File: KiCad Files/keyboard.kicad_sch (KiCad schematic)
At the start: 193 parts, among them J2 Button, J3 78171-0004, J5 Conn_01x03_Male, U1 SOT-23-5 5.5V 3.3V 500mA, U2 RP2040, Y1 3225_4P 12MHz

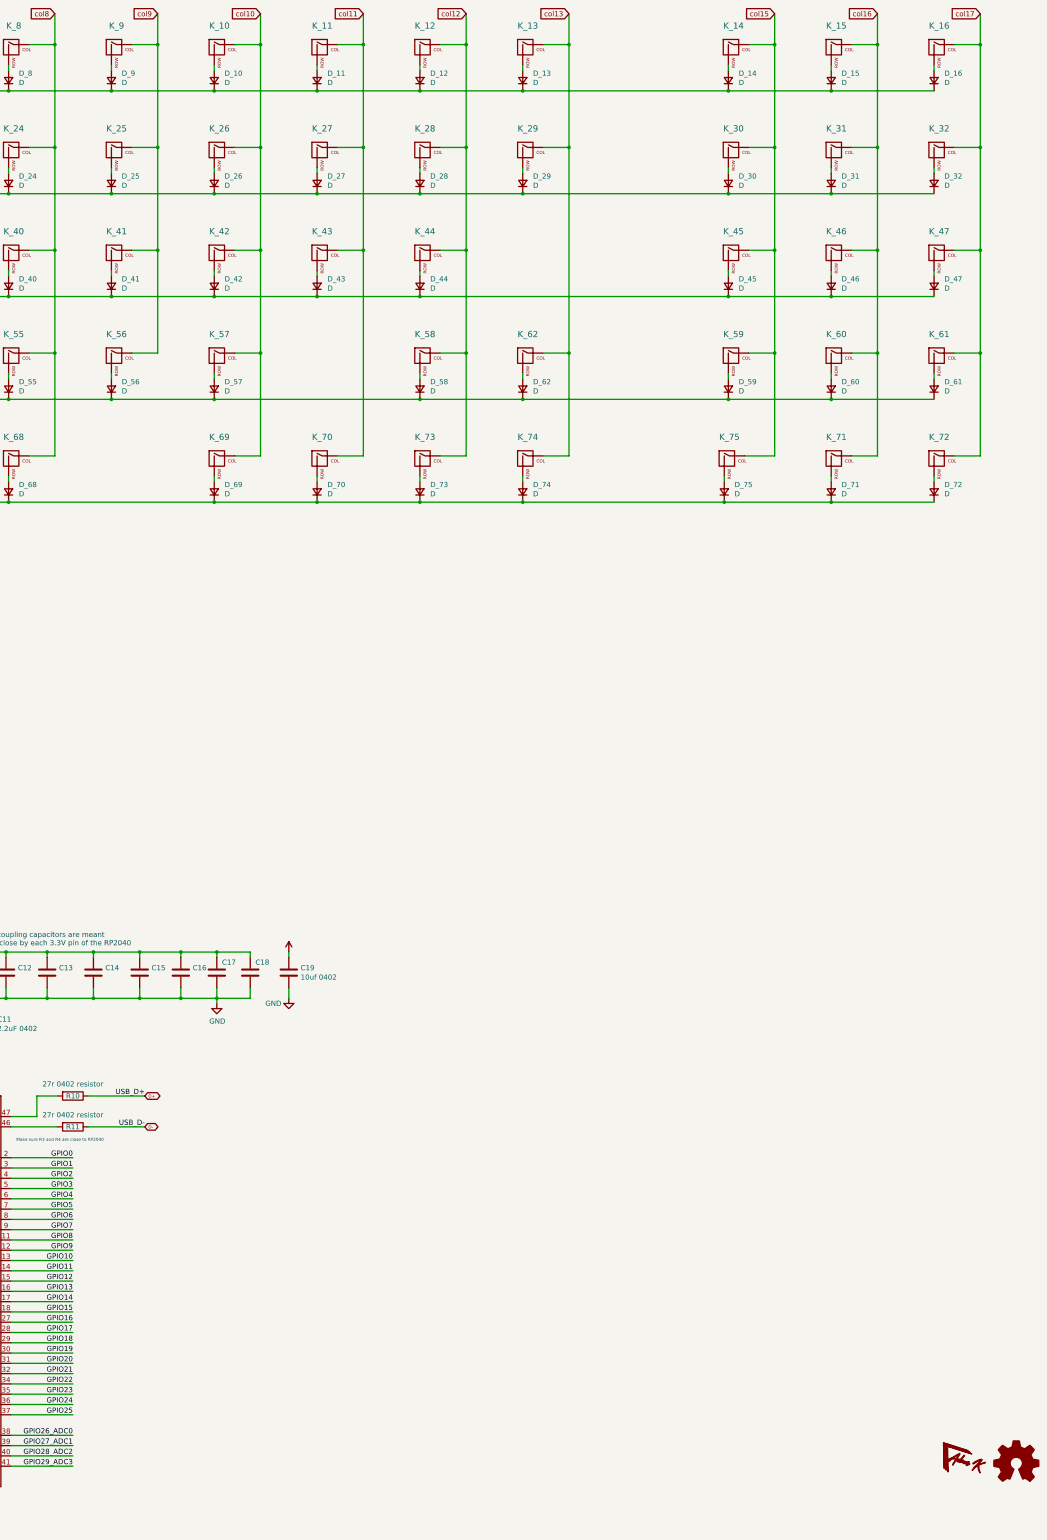
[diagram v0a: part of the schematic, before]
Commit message: routed matrix and updated git ignore
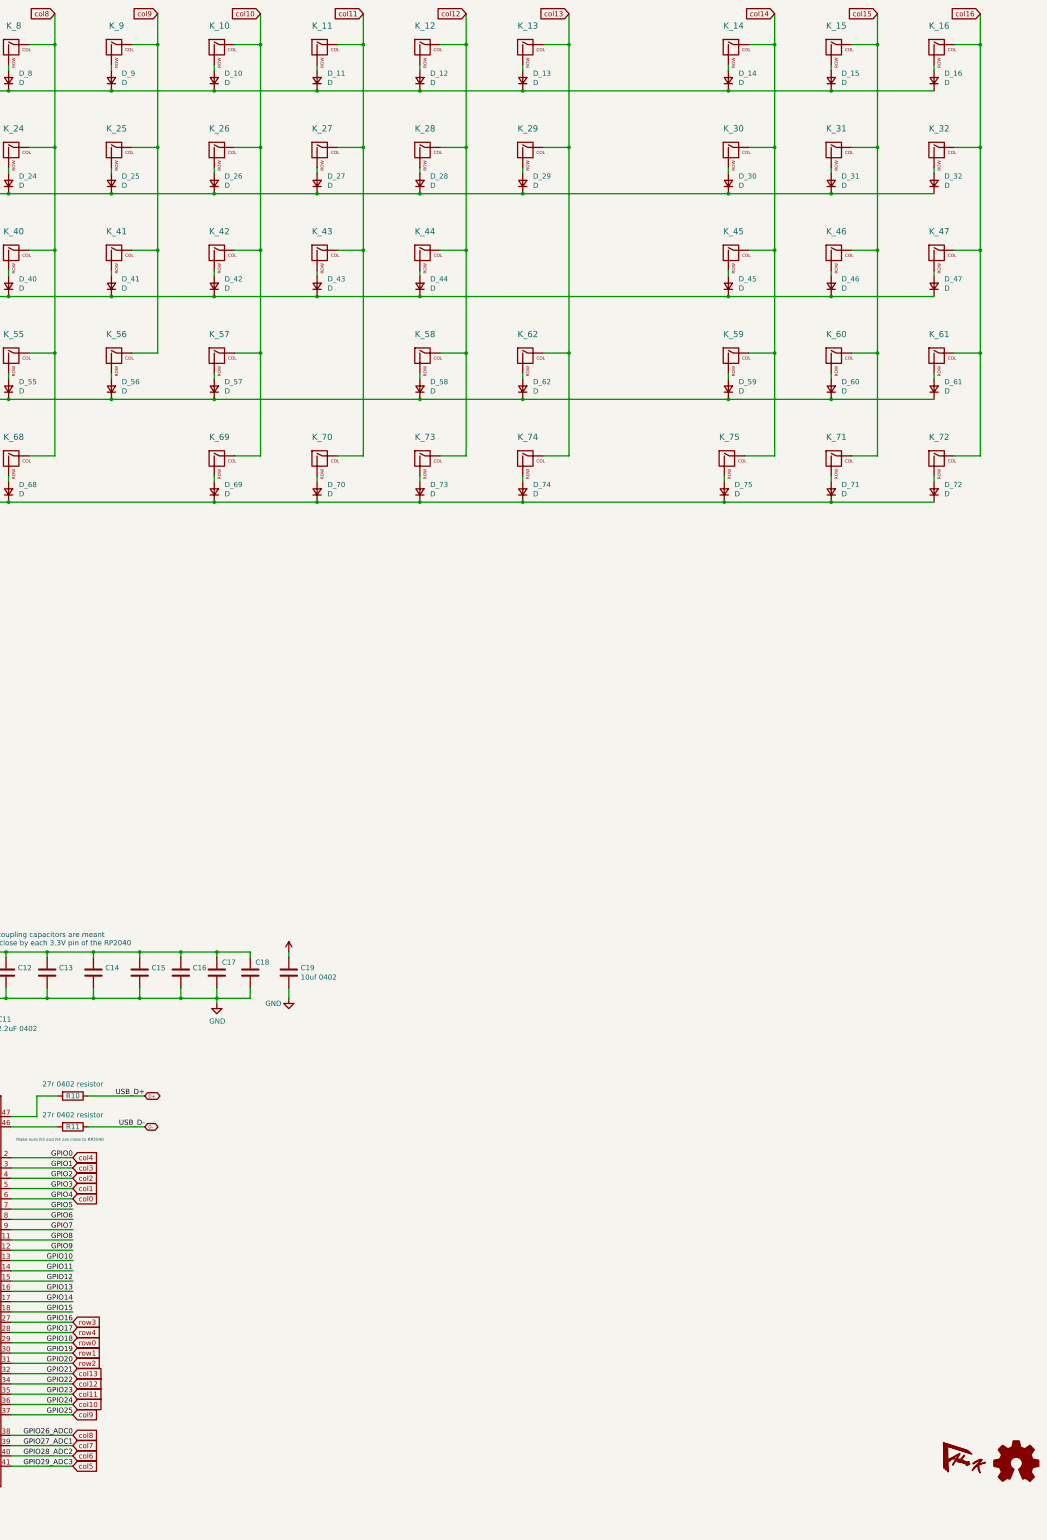
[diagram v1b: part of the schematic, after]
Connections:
- net GPIO0 is gone; now on net col4: U2.2 (GPIO0)
- net GPIO1 is gone; now on net col3: U2.3 (GPIO1)
- net GPIO16 is gone; now on net row3: U2.27 (GPIO16)
- net GPIO17 is gone; now on net row4: U2.28 (GPIO17)
- net GPIO18 is gone; now on net row0: U2.29 (GPIO18)
- net GPIO19 is gone; now on net row1: U2.30 (GPIO19)
- net GPIO2 is gone; now on net col2: U2.4 (GPIO2)
- net GPIO20 is gone; now on net row2: U2.31 (GPIO20)
- net GPIO21 is gone; now on net col13: U2.32 (GPIO21)
- net GPIO22 is gone; now on net col12: U2.34 (GPIO22)
- net GPIO23 is gone; now on net col11: U2.35 (GPIO23)
- net GPIO24 is gone; now on net col10: U2.36 (GPIO24)
- net GPIO25 is gone; now on net col9: U2.37 (GPIO25)
- net GPIO26_ADC0 is gone; now on net col8: U2.38 (GPIO26_ADC0)
- net GPIO27_ADC1 is gone; now on net col7: U2.39 (GPIO27_ADC1)
- net GPIO28_ADC2 is gone; now on net col6: U2.40 (GPIO28_ADC2)
- net GPIO29_ADC3 is gone; now on net col5: U2.41 (GPIO29_ADC3)
- net GPIO3 is gone; now on net col1: U2.5 (GPIO3)
- net GPIO4 is gone; now on net col0: U2.6 (GPIO4)
- net col17 is gone; now on net col16: K_16.1 (COL), K_32.1 (COL), K_47.1 (COL), K_61.1 (COL), K_72.1 (COL)
- net col15: now also K_15.1 (COL), K_31.1 (COL), K_46.1 (COL), K_60.1 (COL), K_71.1 (COL); no longer K_14.1 (COL), K_30.1 (COL), K_45.1 (COL), K_59.1 (COL), K_75.1 (COL)
- net col16: no longer K_15.1 (COL), K_31.1 (COL), K_46.1 (COL), K_60.1 (COL), K_71.1 (COL)
- new net col14: K_14.1 (COL), K_30.1 (COL), K_45.1 (COL), K_59.1 (COL), K_75.1 (COL)
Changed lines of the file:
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@@
     (effects (font (size 1.27 1.27)) (justify right bottom))
   )
+  (global_label "col12" (shape input) (at 262.255 365.125 0)
+    (effects (font (size 1.27 1.27)) (justify left))
+    (property "Intersheetrefs" "${INTERSHEET_REFS}" (at 262.255 365.125 0)
+      (effects (font (size 1.27 1.27)) hide)
+    )
+  )
   (global_label "col11" (shape input) (at 334.01 26.67 180)
     (effects (font (size 1.27 1.27)) (justify right))
@@
     )
   )
+  (global_label "row2" (shape input) (at 262.255 360.045 0)
+    (effects (font (size 1.27 1.27)) (justify left))
+    (property "Intersheetrefs" "${INTERSHEET_REFS}" (at 262.255 360.045 0)
+      (effects (font (size 1.27 1.27)) hide)
+    )
+  )
   (global_label "col1" (shape input) (at 80.01 26.67 180)
     (effects (font (size 1.27 1.27)) (justify right))
@@
     (effects (font (size 1.27 1.27)) (justify right))
     (property "Intersheetrefs" "${INTERSHEET_REFS}" (at 130.81 26.67 0)
+      (effects (font (size 1.27 1.27)) hide)
+    )
+  )
+  (global_label "col0" (shape input) (at 262.255 319.405 0)
+    (effects (font (size 1.27 1.27)) (justify left))
+    (property "Intersheetrefs" "${INTERSHEET_REFS}" (at 262.255 319.405 0)
       (effects (font (size 1.27 1.27)) hide)
     )
@@
     )
   )
+  (global_label "row4" (shape input) (at 262.255 352.425 0)
+    (effects (font (size 1.27 1.27)) (justify left))
+    (property "Intersheetrefs" "${INTERSHEET_REFS}" (at 262.255 352.425 0)
+      (effects (font (size 1.27 1.27)) hide)
+    )
+  )
   (global_label "D-" (shape bidirectional) (at 280.035 301.625 0) (fields_autoplaced)
     (effects (font (size 0.762 0.762)) (justify left))
@@
     )
   )
+  (global_label "col6" (shape input) (at 262.255 382.905 0)
+    (effects (font (size 1.27 1.27)) (justify left))
+    (property "Intersheetrefs" "${INTERSHEET_REFS}" (at 262.255 382.905 0)
+      (effects (font (size 1.27 1.27)) hide)
+    )
+  )
   (global_label "col13" (shape input) (at 384.81 26.67 180)
     (effects (font (size 1.27 1.27)) (justify right))
@@
     )
   )
-  (global_label "col17" (shape input) (at 486.41 26.67 180)
+  (global_label "col1" (shape input) (at 262.255 316.865 0)
+    (effects (font (size 1.27 1.27)) (justify left))
+    (property "Intersheetrefs" "${INTERSHEET_REFS}" (at 262.255 316.865 0)
+      (effects (font (size 1.27 1.27)) hide)
+    )
+  )
+  (global_label "col16" (shape input) (at 486.41 26.67 180)
     (effects (font (size 1.27 1.27)) (justify right))
     (property "Intersheetrefs" "${INTERSHEET_REFS}" (at 486.41 26.67 0)
@@
     (property "Intersheetrefs" "${INTERSHEET_REFS}" (at 283.7108 294.005 0)
       (effects (font (size 0.762 0.762)) (justify left) hide)
+    )
+  )
+  (global_label "col7" (shape input) (at 262.255 380.365 0)
+    (effects (font (size 1.27 1.27)) (justify left))
+    (property "Intersheetrefs" "${INTERSHEET_REFS}" (at 262.255 380.365 0)
+      (effects (font (size 1.27 1.27)) hide)
     )
   )
@@
     )
   )
+  (global_label "col8" (shape input) (at 262.255 377.825 0)
+    (effects (font (size 1.27 1.27)) (justify left))
+    (property "Intersheetrefs" "${INTERSHEET_REFS}" (at 262.255 377.825 0)
+      (effects (font (size 1.27 1.27)) hide)
+    )
+  )
   (global_label "XIN" (shape input) (at 85.725 383.54 0) (fields_autoplaced)
     (effects (font (size 1.27 1.27)) (justify left))
@@
     )
   )
+  (global_label "col2" (shape input) (at 262.255 314.325 0)
+    (effects (font (size 1.27 1.27)) (justify left))
+    (property "Intersheetrefs" "${INTERSHEET_REFS}" (at 262.255 314.325 0)
+      (effects (font (size 1.27 1.27)) hide)
+    )
+  )
   (global_label "row3" (shape input) (at 31.75 121.92 180)
     (effects (font (size 1.27 1.27)) (justify right))
@@
     )
   )
-  (global_label "col15" (shape input) (at 435.61 26.67 180)
+  (global_label "col14" (shape input) (at 435.61 26.67 180)
     (effects (font (size 1.27 1.27)) (justify right))
     (property "Intersheetrefs" "${INTERSHEET_REFS}" (at 435.61 26.67 0)
@@
     )
   )
-  (global_label "col16" (shape input) (at 461.01 26.67 180)
+  (global_label "row3" (shape input) (at 262.255 349.885 0)
+    (effects (font (size 1.27 1.27)) (justify left))
+    (property "Intersheetrefs" "${INTERSHEET_REFS}" (at 262.255 349.885 0)
+      (effects (font (size 1.27 1.27)) hide)
+    )
+  )
+  (global_label "col3" (shape input) (at 262.255 311.785 0)
+    (effects (font (size 1.27 1.27)) (justify left))
+    (property "Intersheetrefs" "${INTERSHEET_REFS}" (at 262.255 311.785 0)
+      (effects (font (size 1.27 1.27)) hide)
+    )
+  )
+  (global_label "col11" (shape input) (at 262.255 367.665 0)
+    (effects (font (size 1.27 1.27)) (justify left))
+    (property "Intersheetrefs" "${INTERSHEET_REFS}" (at 262.255 367.665 0)
+      (effects (font (size 1.27 1.27)) hide)
+    )
+  )
+  (global_label "col10" (shape input) (at 262.255 370.205 0)
+    (effects (font (size 1.27 1.27)) (justify left))
+    (property "Intersheetrefs" "${INTERSHEET_REFS}" (at 262.255 370.205 0)
+      (effects (font (size 1.27 1.27)) hide)
+    )
+  )
+  (global_label "col15" (shape input) (at 461.01 26.67 180)
     (effects (font (size 1.27 1.27)) (justify right))
     (property "Intersheetrefs" "${INTERSHEET_REFS}" (at 461.01 26.67 0)
@@
     )
   )
+  (global_label "row1" (shape input) (at 262.255 357.505 0)
+    (effects (font (size 1.27 1.27)) (justify left))
+    (property "Intersheetrefs" "${INTERSHEET_REFS}" (at 262.255 357.505 0)
+      (effects (font (size 1.27 1.27)) hide)
+    )
+  )
+  (global_label "col9" (shape input) (at 262.255 372.745 0)
+    (effects (font (size 1.27 1.27)) (justify left))
+    (property "Intersheetrefs" "${INTERSHEET_REFS}" (at 262.255 372.745 0)
+      (effects (font (size 1.27 1.27)) hide)
+    )
+  )
   (global_label "row2" (shape input) (at 31.75 96.52 180)
     (effects (font (size 1.27 1.27)) (justify right))
@@
     )
   )
+  (global_label "col5" (shape input) (at 262.255 385.445 0)
+    (effects (font (size 1.27 1.27)) (justify left))
+    (property "Intersheetrefs" "${INTERSHEET_REFS}" (at 262.255 385.445 0)
+      (effects (font (size 1.27 1.27)) hide)
+    )
+  )
   (global_label "5V" (shape input) (at 35.56 228.6 90) (fields_autoplaced)
     (effects (font (size 0.762 0.762)) (justify left))
     (property "Intersheetrefs" "${INTERSHEET_REFS}" (at 35.56 225.8223 90)
       (effects (font (size 0.762 0.762)) (justify left) hide)
+    )
+  )
+  (global_label "col13" (shape input) (at 262.255 362.585 0)
+    (effects (font (size 1.27 1.27)) (justify left))
+    (property "Intersheetrefs" "${INTERSHEET_REFS}" (at 262.255 362.585 0)
+      (effects (font (size 1.27 1.27)) hide)
     )
   )
@@
     )
   )
+  (global_label "row0" (shape input) (at 262.255 354.965 0)
+    (effects (font (size 1.27 1.27)) (justify left))
+    (property "Intersheetrefs" "${INTERSHEET_REFS}" (at 262.255 354.965 0)
+      (effects (font (size 1.27 1.27)) hide)
+    )
+  )
   (global_label "col8" (shape input) (at 257.81 26.67 180)
     (effects (font (size 1.27 1.27)) (justify right))
@@
       (effects (font (size 1.27 1.27)) hide)
     )
+  )
+  (global_label "col4" (shape input) (at 262.255 309.245 0)
+    (effects (font (size 1.27 1.27)) (justify left))
+    (property "Intersheetrefs" "${INTERSHEET_REFS}" (at 262.255 309.245 0)
+      (effects (font (size 1.27 1.27)) hide)
+    )

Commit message: added silkscreen markings, broke out unused GPIOs, cleaned up board, ran DRC and cleaned up traces.
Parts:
- added C1, C20: 100nf 0402, Capacitor_SMD:C_0402_1005Metric, symbol Device:C_Small
- added GTP1, GTP2, GTP3, GTP4: GNDPAD, Connector_Wire:SolderWire-0.1sqmm_1x01_D0.4mm_OD1mm, symbol Connector:TestPoint
- added J1: Conn_01x10, Connector_PinHeader_1.00mm:PinHeader_1x10_P1.00mm_Vertical, symbol Connector_Generic:Conn_01x10
- added U3: TXS0101DCK, Package_TO_SOT_SMD:SOT-363_SC-70-6, symbol Logic_LevelTranslator:TXS0101DCK
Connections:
- net VSYS is gone; now on net +5V: C5.1, F1.1, U1.1 (IN)
- net +3V3: now also C1.1, U3.1 (V_{CCA}), U3.5 (OE)
- net GND: now also D1.1 (VSS), D2.1 (VSS), D3.1 (VSS), C1.2, C20.2, GTP1.1, GTP2.1, GTP3.1, GTP4.1, U3.2 (GND)
- net GPIO10: now also J1.5 (Pin_5)
- net GPIO11: now also J1.6 (Pin_6)
- net GPIO12: now also J1.7 (Pin_7)
- net GPIO13: now also J1.8 (Pin_8)
- net GPIO14: now also J1.9 (Pin_9)
- net GPIO15: now also J1.10 (Pin_10)
- net GPIO6: now also J1.1 (Pin_1)
- net GPIO7: now also J1.2 (Pin_2)
- net GPIO8: now also J1.3 (Pin_3)
- net GPIO9: now also J1.4 (Pin_4)
- net +5V: now reaches D3.3 (VDD)
- net +5V: now also D1.3 (VDD), D2.3 (VDD), C20.1, U3.6 (V_{CCB})
- net RGB_DATA_5V0: now reaches D1.2 (DIN)
- net RGB_DATA_5V0: now also U3.4 (B)
- net 5V renamed VBUS
- net GPIO5 renamed RGB_DATA_3V3
- net RGB_DATA_3V3: now also U3.3 (A)
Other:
- moved on the sheet: D1, D2, D3, F1

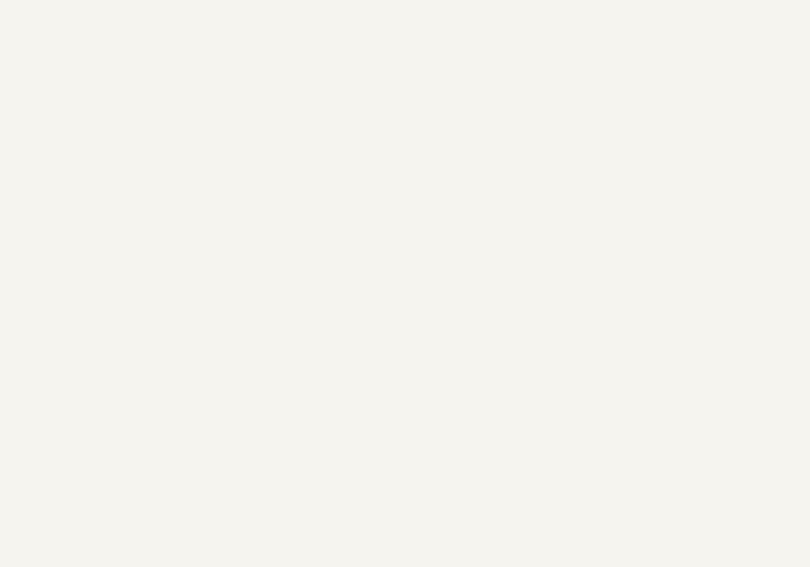
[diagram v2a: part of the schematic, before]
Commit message: added test points, cleaned up PCB, Generated production files
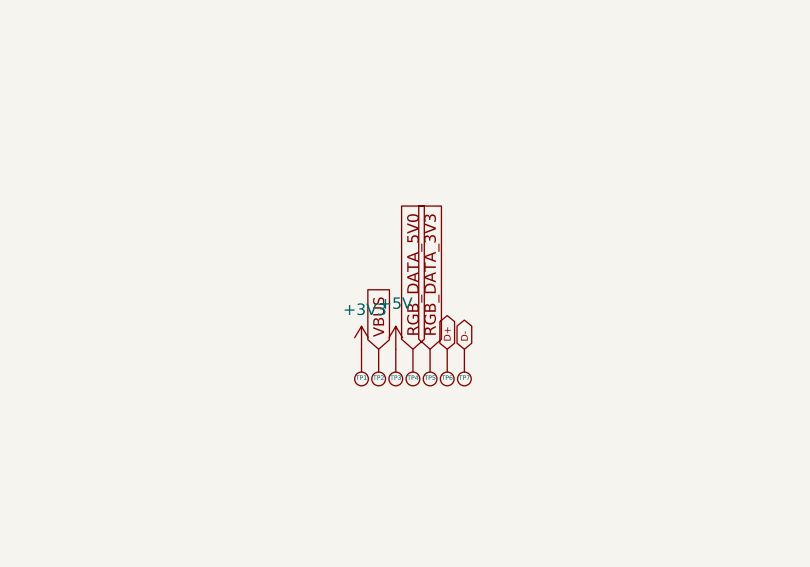
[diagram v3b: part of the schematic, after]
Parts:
- added TP1, TP2, TP3, TP4, TP5, TP6, TP7: TestPoint, TestPoint:TestPoint_Pad_D1.0mm, symbol Connector:TestPoint
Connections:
- net +3V3: now also TP1.1
- net +5V: now also TP3.1
- net D+: now also TP6.1
- net D-: now also TP7.1
- net RGB_DATA_3V3: now also TP5.1
- net RGB_DATA_5V0: now also TP4.1
- net VBUS: now also TP2.1
